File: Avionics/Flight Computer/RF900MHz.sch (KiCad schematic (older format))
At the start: 47 parts, among them J4 734120110, U1 CC1310F128RGZR, U2 CC1190RGVR, Y3 XRCGB24M000F2P00R0

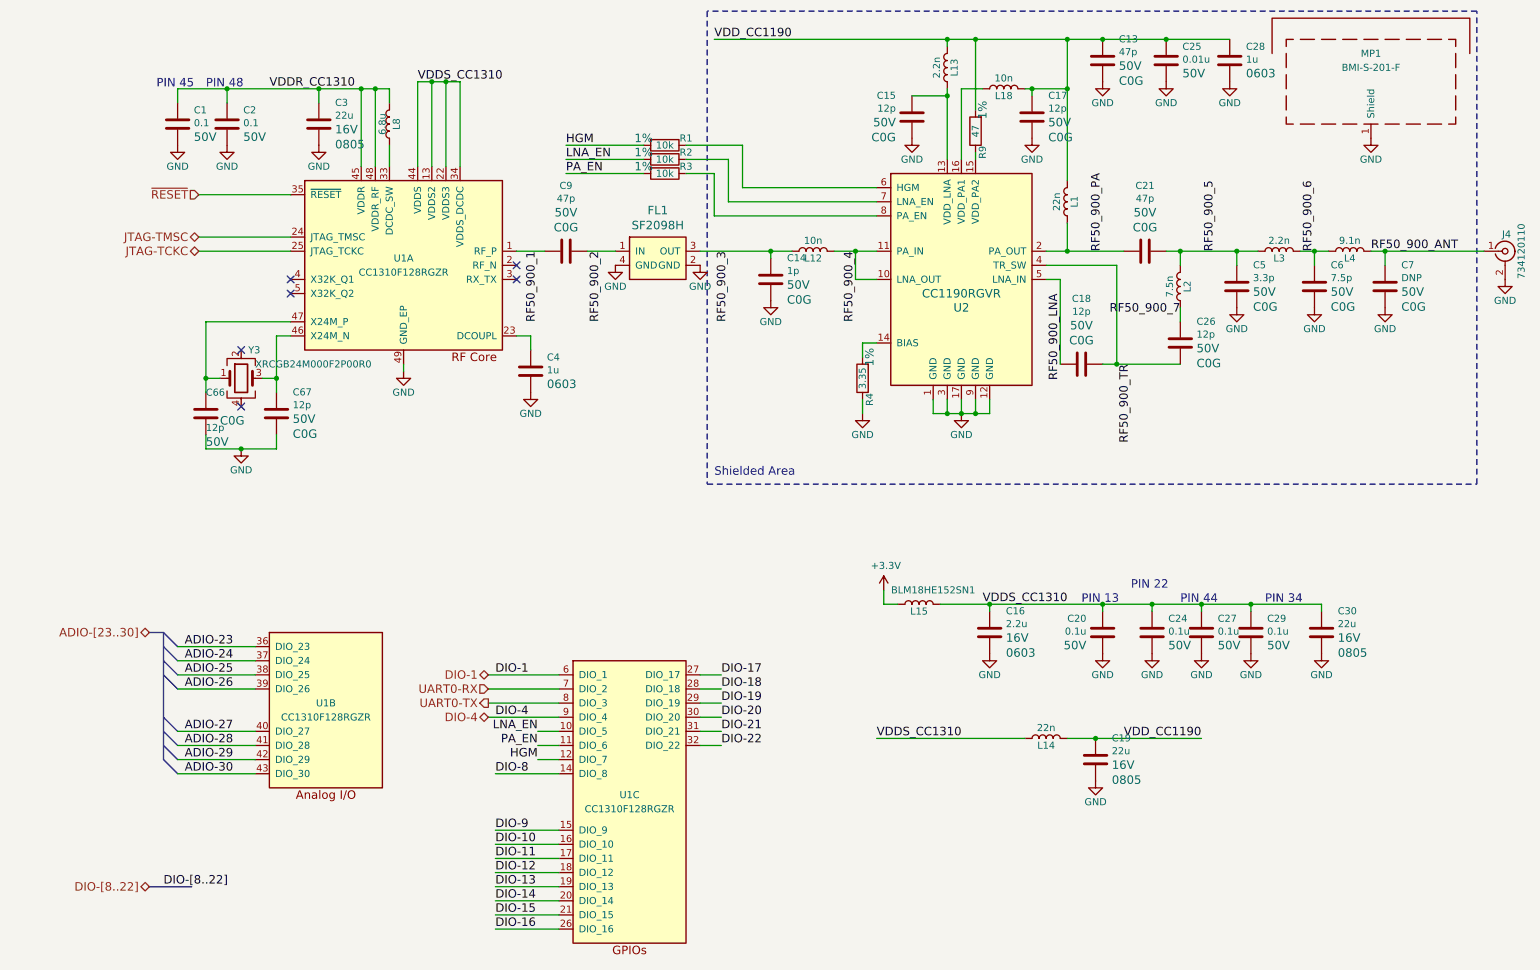
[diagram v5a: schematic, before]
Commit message: Wired up everything and started rearranging layout
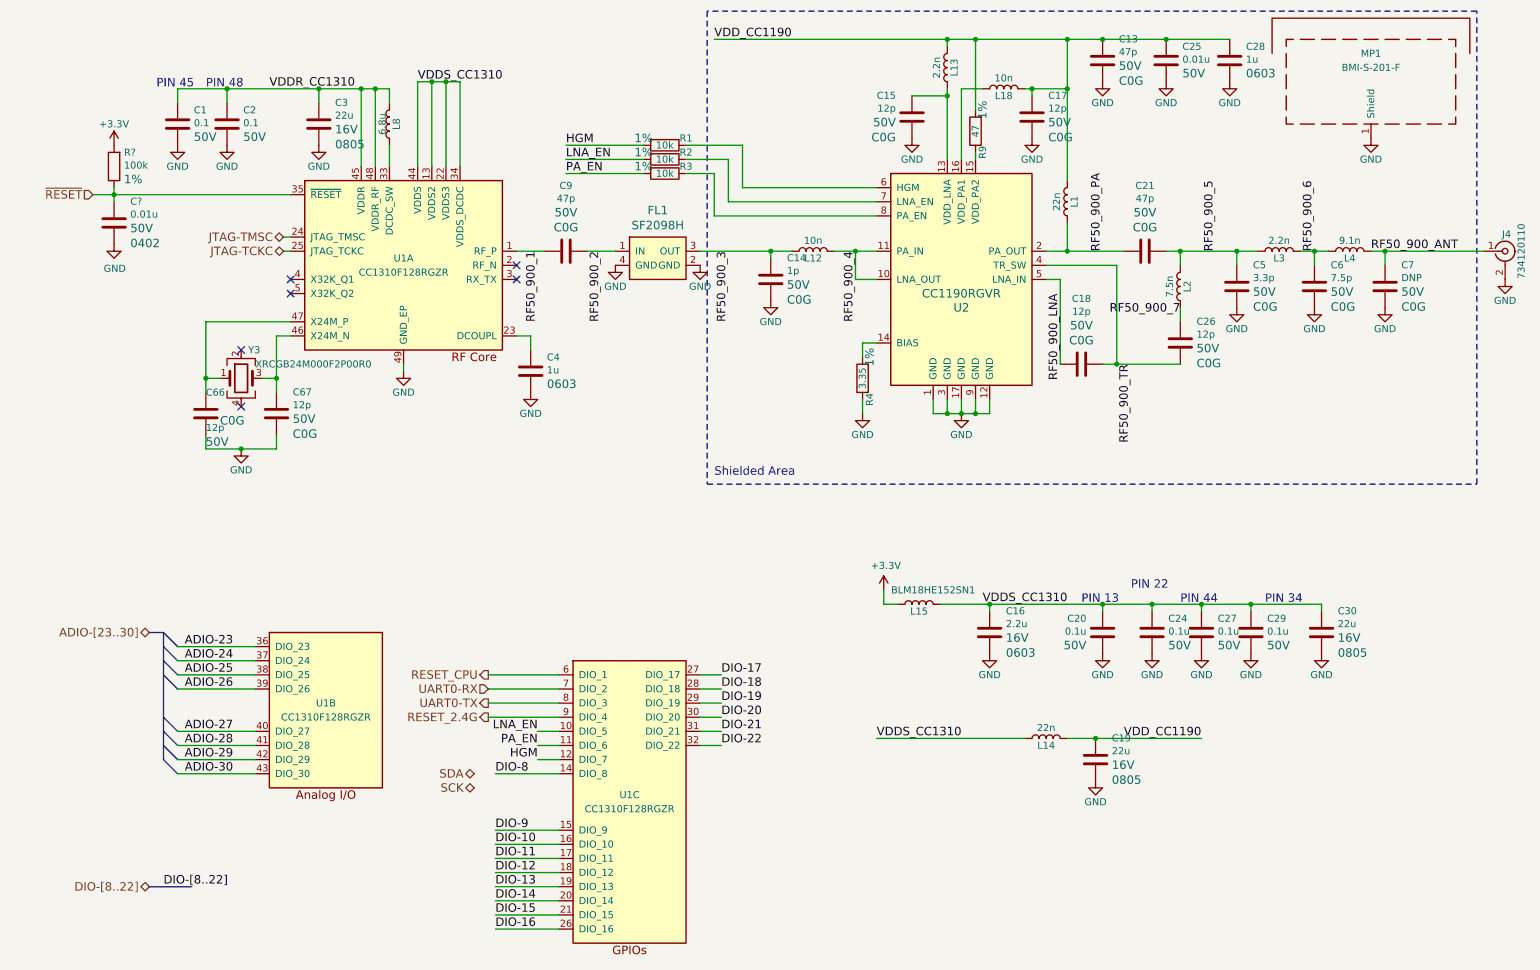
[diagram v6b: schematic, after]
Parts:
- added C?: 0.01u, Capacitors_SMD:C_0402, symbol C
- added R?: 100k, Resistors_SMD:R_0402, symbol R
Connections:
- net labels added: RESET_2.4G, RESET_CPU, SCK, SDA
- net labels removed: DIO-1, DIO-4
- wire segments 123 -> 160
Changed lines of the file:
@@
 $Descr A4 11693 8268
 encoding utf-8
-Sheet 3 9
+Sheet 3 8
 Title ""
 Date ""
@@
 	7750 2500 7650 2500
 Wire Wire Line
-	8050 3100 8600 3100
+	8050 3100 8150 3100
+Wire Wire Line
+	8150 3100 8600 3100
 Wire Wire Line
 	8600 2800 8600 2700
 Wire Wire Line
-	7650 2300 8200 2300
+	7650 2300 7800 2300
+Wire Wire Line
+	7800 2300 8200 2300
 Wire Wire Line
 	7800 2100 7800 2300
 Connection ~ 7800 2300
 Wire Wire Line
-	8500 2300 9150 2300
+	8500 2300 8600 2300
+Wire Wire Line
+	8600 2300 9000 2300
+Wire Wire Line
+	9000 2300 9150 2300
 Wire Wire Line
 	8600 2400 8600 2300
@@
 Connection ~ 8150 3100
 Wire Wire Line
-	9450 2300 9650 2300
-Wire Wire Line
-	9950 2300 10750 2300
+	9450 2300 9550 2300
+Wire Wire Line
+	9550 2300 9650 2300
+Wire Wire Line
+	9950 2300 10050 2300
+Wire Wire Line
+	10050 2300 10750 2300
 Wire Wire Line
 	10050 2400 10050 2300
@@
 Connection ~ 9000 2300
 Wire Wire Line
-	7800 800  7800 1800
+	7800 800  7800 1150
+Wire Wire Line
+	7800 1150 7800 1800
 Wire Wire Line
 	6850 3350 6850 3450
 Wire Wire Line
-	6850 3450 7250 3450
+	6850 3450 6950 3450
+Wire Wire Line
+	6950 3450 7050 3450
+Wire Wire Line
+	7050 3450 7150 3450
+Wire Wire Line
+	7150 3450 7250 3450
 Wire Wire Line
 	7250 3450 7250 3350
@@
 	6300 2500 6450 2500
 Wire Wire Line
-	6150 2300 6450 2300
+	6150 2300 6300 2300
+Wire Wire Line
+	6300 2300 6450 2300
 Wire Notes Line
 	5250 600  5250 3950
@@
 	6350 2950 6450 2950
 Wire Wire Line
-	6900 4800 9600 4800
-Wire Wire Line
-	5300 800  8950 800
+	6900 4800 7250 4800
+Wire Wire Line
+	7250 4800 8050 4800
+Wire Wire Line
+	8050 4800 8400 4800
+Wire Wire Line
+	8400 4800 8750 4800
+Wire Wire Line
+	8750 4800 9100 4800
+Wire Wire Line
+	9100 4800 9600 4800
+Wire Wire Line
+	5300 800  6950 800
+Wire Wire Line
+	6950 800  7150 800
+Wire Wire Line
+	7150 800  7800 800
+Wire Wire Line
+	7800 800  8050 800
+Wire Wire Line
+	8050 800  8500 800
+Wire Wire Line
+	8500 800  8950 800
 Wire Wire Line
 	6500 4700 6500 4800
@@
 	3500 1100 3500 1700
 Wire Wire Line
-	3200 1100 3500 1100
+	3200 1100 3300 1100
+Wire Wire Line
+	3300 1100 3400 1100
+Wire Wire Line
+	3400 1100 3500 1100
 Wire Wire Line
 	3200 1100 3200 1700
@@
 	3000 1150 3000 1250
 Wire Wire Line
-	1500 1150 3000 1150
+	1500 1150 1850 1150
+Wire Wire Line
+	1850 1150 2500 1150
+Wire Wire Line
+	2500 1150 2800 1150
+Wire Wire Line
+	2800 1150 2900 1150
+Wire Wire Line
+	2900 1150 3000 1150
 Wire Wire Line
 	2500 1150 2500 1250
@@
 Connection ~ 8050 800
 Wire Wire Line
-	7500 1150 7800 1150
+	7500 1150 7550 1150
+Wire Wire Line
+	7550 1150 7800 1150
 Connection ~ 7800 1150
 $Comp
@@
 	6700 1200 6950 1200
 Wire Wire Line
-	6950 1150 6950 1650
+	6950 1150 6950 1200
+Wire Wire Line
+	6950 1200 6950 1650
 Connection ~ 6950 1200
 Text Label 6450 5750 0    60   ~ 0
@@
 	6450 5750 7500 5750
 Wire Wire Line
-	7800 5750 8750 5750
+	7800 5750 8000 5750
+Wire Wire Line
+	8000 5750 8750 5750
 $Comp
 L L L14
@@
 	5700 2350 5700 2300
 Wire Wire Line
-	5200 2300 5850 2300
+	5200 2300 5700 2300
+Wire Wire Line
+	5700 2300 5850 2300
 Connection ~ 5700 2300
 $Comp
@@
 	1700 3600 1700 3700
 Wire Wire Line
-	1700 3700 2200 3700
+	1700 3700 1950 3700
+Wire Wire Line
+	1950 3700 2200 3700
 Wire Wire Line
 	2200 3700 2200 3600
@@
 	1800 3200 1700 3200
 Wire Wire Line
-	1700 2800 1700 3300
+	1700 2800 1700 3200
+Wire Wire Line
+	1700 3200 1700 3300
 Wire Wire Line
 	2100 3200 2200 3200
 Wire Wire Line
-	2200 2900 2200 3300
+	2200 2900 2200 3200
+Wire Wire Line
+	2200 3200 2200 3300
 Wire Wire Line
 	2200 2900 2300 2900
@@
 	1400 5000 1500 5100
 Wire Bus Line
-	1400 5000 1400 5900
+	1400 5000 1400 5100
+Wire Bus Line
+	1400 5100 1400 5200
+Wire Bus Line
+	1400 5200 1400 5300
+Wire Bus Line
+	1400 5300 1400 5600
+Wire Bus Line
+	1400 5600 1400 5700
+Wire Bus Line
+	1400 5700 1400 5800
+Wire Bus Line
+	1400 5800 1400 5900
 Wire Bus Line
 	1400 5000 1300 5000
@@
 Text Label 1550 6000 0    60   ~ 0
 ADIO-30
-Text HLabel 1650 1900 0    60   Input ~ 0
-~RESET
-Wire Wire Line
-	1650 1900 2300 1900
-Wire Wire Line
-	1650 2200 2300 2200
-Wire Wire Line
-	1650 2300 2300 2300
-Text HLabel 1650 2200 0    60   BiDi ~ 0
+Wire Wire Line
+	2250 2200 2300 2200
+Wire Wire Line
+	2250 2300 2300 2300
+Text HLabel 2250 2200 0    60   BiDi ~ 0
 JTAG-TMSC
-Text HLabel 1650 2300 0    60   BiDi ~ 0
+Text HLabel 2250 2300 0    60   BiDi ~ 0
 JTAG-TCKC
 Text HLabel 1300 6800 0    60   BiDi ~ 0
@@
 NoConn ~ 3900 2400
 NoConn ~ 3900 2500
-Text Label 3750 5300 0    60   ~ 0
-DIO-1
 Wire Wire Line
 	3700 5300 4200 5300
-Text Label 3750 5600 0    60   ~ 0
-DIO-4
 Wire Wire Line
 	3700 5600 4200 5600
@@
 Wire Wire Line
 	4200 6500 3750 6500
-Text HLabel 3700 5600 0    60   BiDi ~ 0
-DIO-4
-Text HLabel 3700 5300 0    60   BiDi ~ 0
-DIO-1
+Text HLabel 3700 5600 0    60   Output ~ 0
+RESET_2.4G
+Text HLabel 3700 5300 0    60   Output ~ 0
+RESET_CPU
+Text HLabel 3600 6000 0    60   BiDi ~ 0
+SDA
+Text HLabel 3600 6100 0    60   BiDi ~ 0
+SCK
+Text HLabel 900  1900 0    60   Input ~ 0
+~RESET
+Wire Wire Line
+	900  1900 1050 1900
+Wire Wire Line
+	1050 1900 2300 1900
+$Comp
+L C C?
+U 1 1 58C2B894
+P 1050 2100
+F 0 "C?" H 1165 2252 50  0000 L CNN
+F 1 "0.01u" H 1165 2161 50  0000 L CNN
+F 2 "Capacitors_SMD:C_0402" H -4662 -750 50  0001 C CNN
+F 3 "" H -4700 -600 50  0001 C CNN
+F 4 "50V" H 1165 2062 60  0000 L CNN "Voltage"
+F 5 "20%" H 1165 2009 60  0001 L CNN "Tolerance"
+F 6 "X7R" H 1165 1956 60  0001 L CNN "Type"
+F 7 "0402" H 1165 1956 60  0000 L CNN "Package"
+	1    1050 2100
+	1    0    0    -1
+$EndComp
+$Comp
+L GND #PWR?
+U 1 1 58C2B89B
+P 1050 2250
+F 0 "#PWR?" H 1100 2300 50  0001 C CNN
+F 1 "GND" H 1055 2077 50  0000 C CNN
+F 2 "" H -5750 -1500 50  0001 C CNN
+F 3 "" H -5750 -1500 50  0001 C CNN
+	1    1050 2250
+	1    0    0    -1
+$EndComp
+Wire Wire Line
+	1050 1850 1050 1900
+Wire Wire Line
+	1050 1900 1050 1950
+Connection ~ 1050 1900
+$Comp
+L R R?
+U 1 1 58C2B8A9
+P 1050 1700
+F 0 "R?" H 980 1601 50  0000 R CNN
+F 1 "100k" H 980 1692 50  0000 R CNN
+F 2 "Resistors_SMD:R_0402" V -3950 400 50  0001 C CNN
+F 3 "" V -3670 400 50  0001 C CNN
+F 4 "1%" H 980 1791 60  0000 R CNN "Tolerance"
+F 5 "50V" V -3500 400 60  0001 C CNN "Voltage"
+F 6 "0.062W" V -3400 400 60  0001 C CNN "Power"
+F 7 "Thin Film" V -3300 400 60  0001 C CNN "Material"
+F 8 "0402" V -3850 400 60  0001 C CNN "Package"
+	1    1050 1700
+	-1   0    0    1
+$EndComp
+$Comp
+L +3.3V #PWR?
+U 1 1 58C2B8B0
+P 1050 1550
+F 0 "#PWR?" H 1100 1600 50  0001 C CNN
+F 1 "+3.3V" H 1050 1700 50  0000 C CNN
+F 2 "" H -6300 -3250 50  0001 C CNN
+F 3 "" H -6300 -3250 50  0001 C CNN
+	1    1050 1550
+	1    0    0    -1
+$EndComp
 $EndSCHEMATC

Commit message: Finished breaking out signals to connector sheet and interconnecting processors.
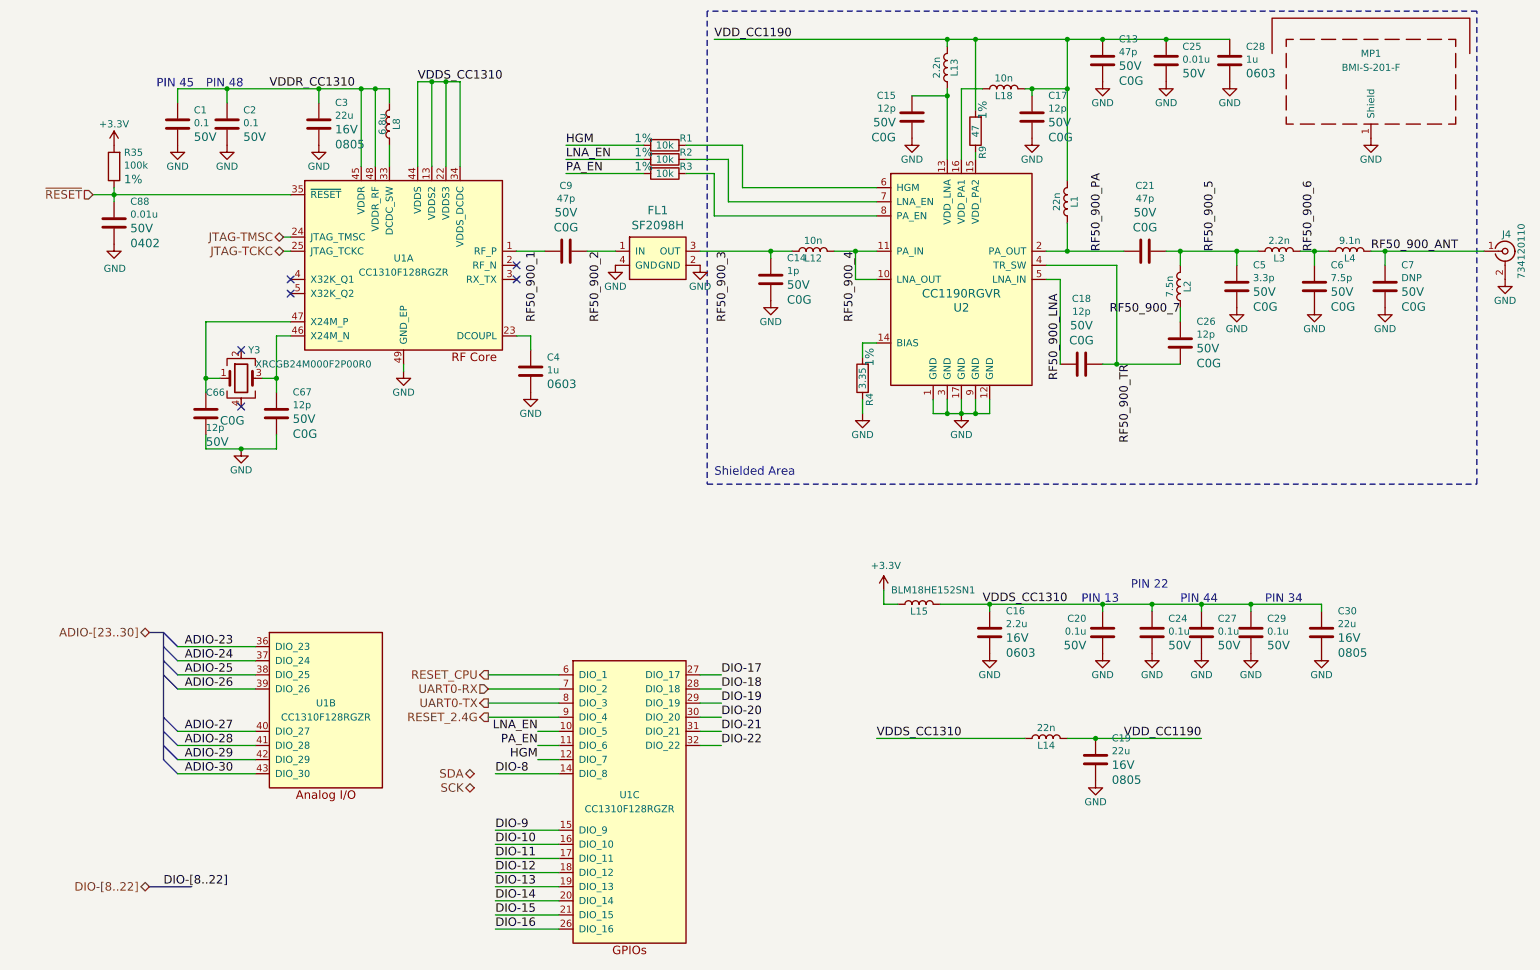
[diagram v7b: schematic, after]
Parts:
- gave numbers to parts that had none: 2
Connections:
- wire segments 160 -> 124

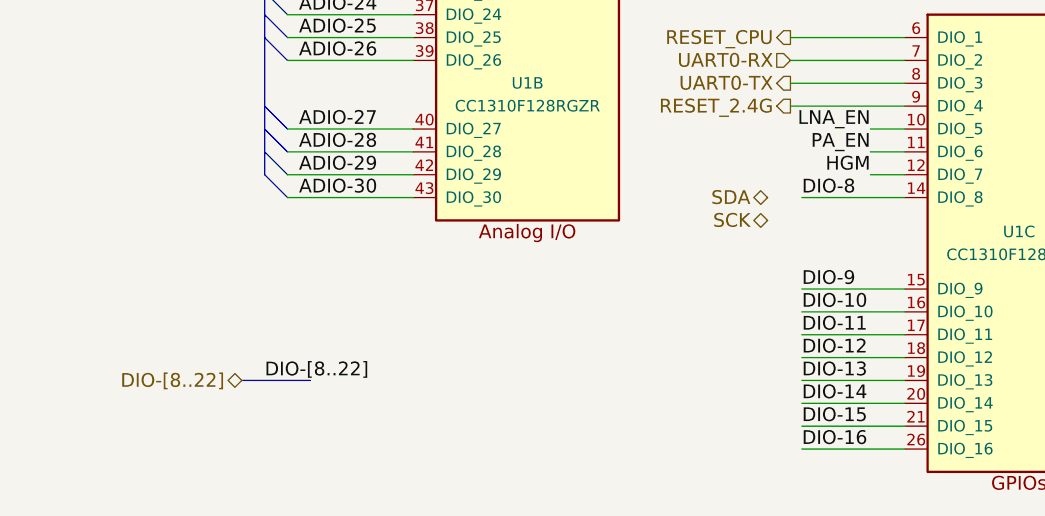
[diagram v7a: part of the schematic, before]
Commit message: Fixed missing connections and did more layout
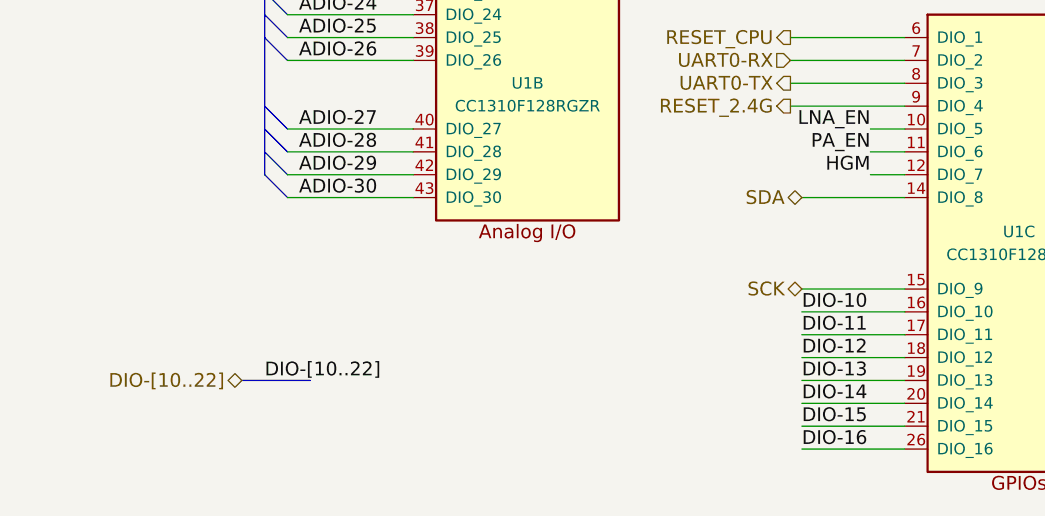
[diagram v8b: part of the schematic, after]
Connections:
- net labels added: DIO-[10..22]
- net labels removed: DIO-8, DIO-9, DIO-[8..22]
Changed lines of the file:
@@
 JTAG-TCKC
 Text HLabel 1300 6800 0    60   BiDi ~ 0
-DIO-[8..22]
+DIO-[10..22]
 Wire Bus Line
 	1300 6800 1600 6800
 Text Label 1400 6800 0    60   ~ 0
-DIO-[8..22]
+DIO-[10..22]
 Text Label 3750 6600 0    60   ~ 0
 DIO-11
@@
 Wire Wire Line
 	3700 5600 4200 5600
-Text Label 3750 6000 0    60   ~ 0
-DIO-8
-Wire Wire Line
-	3750 6000 4200 6000
-Text Label 3750 6400 0    60   ~ 0
-DIO-9
-Text Label 3750 6500 0    60   ~ 0
-DIO-10
 Wire Wire Line
 	3750 6400 4200 6400
@@
 Text HLabel 3700 5300 0    60   Output ~ 0
 RESET_CPU
-Text HLabel 3600 6000 0    60   BiDi ~ 0
+Text HLabel 3750 6000 0    60   BiDi ~ 0
 SDA
-Text HLabel 3600 6100 0    60   BiDi ~ 0
+Text HLabel 3750 6400 0    60   BiDi ~ 0
 SCK
 Text HLabel 900  1900 0    60   Input ~ 0
@@
 	1    0    0    -1
 $EndComp
+Text Label 3750 6500 0    60   ~ 0
+DIO-10
+Wire Wire Line
+	3750 6000 4200 6000
 $EndSCHEMATC
